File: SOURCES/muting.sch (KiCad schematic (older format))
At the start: 39 parts, among them Q1 BSH103,215, Q10 MMBF5434, Q11 MMBF5434, Q12 MMBF5434, Q13 BSS123, Q2 BSH103,215, Q3 BSH103,215, Q4 BSH103,215, Q5 BSH103,215, Q6 BSH103,215, Q7 BSH103,215, Q8 BSH103,215, Q9 MMBF5434, U1 SN74LVC3G14, U2 LM393, U3 LM393

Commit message: Updated schematics and labels
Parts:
- removed R1: 1k, symbol R
- added J4, J5, J6, J7: RCA_01, symbol RCA_01
- Q18: renamed from Q13; footprint (none) -> fdsp_housing_new:SOT-23
- renumbered C1 to C38, C2 to C39, C3 to C40, C4 to C41, C5 to C42, C6 to C43, C7 to C44, C8 to C45, C9 to C46, D5 to D10, D1 to D6, D2 to D7, D3 to D8, D4 to D9, Q5 to Q10, Q6 to Q11, Q7 to Q12, Q8 to Q13, Q9 to Q14, Q10 to Q15, Q11 to Q16, Q12 to Q17, Q1 to Q6, Q2 to Q7, Q3 to Q8, Q4 to Q9, R2 to R36, R3 to R37, R4 to R38, R5 to R39, R6 to R40, R7 to R41, R8 to R42, R9 to R43, U1 to U5, U2 to U6, U3 to U6
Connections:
- net +3V3: now also U6.6 (_); no longer U6.2 (_)
- net GND: now also C40.1, C41.1, U6.5 (+), J4.2 (GND), J5.2 (GND), J6.2 (GND), J7.2 (GND); no longer U6.3 (+)
- net CH1_OUT: no longer names the net of Q10.3 (D), Q14.1 (D)
- net CH1_OUT: now also J4.1 (SIG)
- net CH2_OUT: no longer names the net of Q11.3 (D), Q15.1 (D)
- net CH2_OUT: now also J5.1 (SIG)
- net CH3_OUT: no longer names the net of Q12.3 (D), Q16.1 (D)
- net CH3_OUT: now also J6.1 (SIG)
- net CH4_OUT: no longer names the net of Q13.3 (D), Q17.1 (D)
- net CH4_OUT: now also J7.1 (SIG)
- no-connect marks 0 -> 1

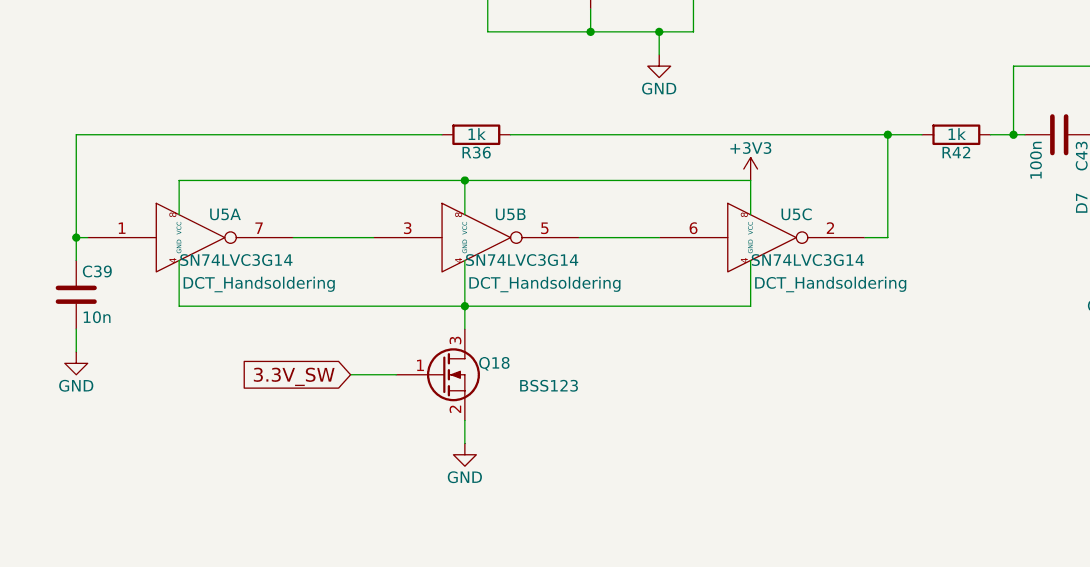
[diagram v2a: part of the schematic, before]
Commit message: Assigned footprints
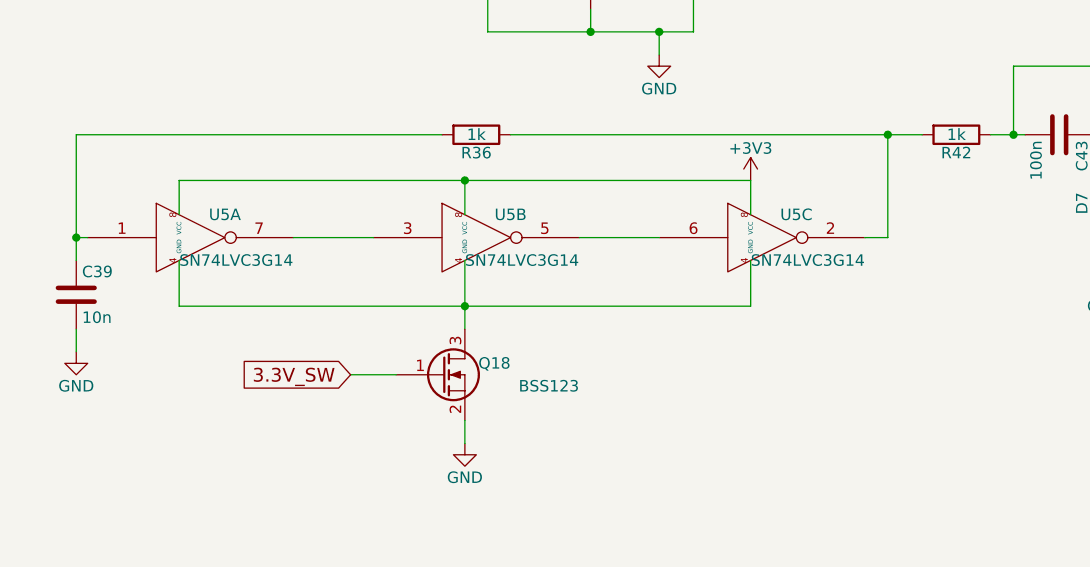
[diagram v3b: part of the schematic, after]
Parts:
- C38, C42: footprint (none) -> fdsp_capacitor:C_Radial_D5_L11_P2
- C39, C40, C41, C43, C44, C45, C46: footprint (none) -> fdsp_capacitor:C_1206_HandSoldering
- D10, D6, D7, D8, D9: footprint (none) -> fdsp_diode:SOD-123W
- J4, J5, J6, J7: footprint (none) -> fdsp_connector:RCA_RCJ-01x
- Q10, Q11, Q12, Q13, Q14, Q15, Q16, Q17, Q6, Q7, Q8, Q9: footprint TO_SOT_Packages_SMD:SOT-23_Handsoldering -> fdsp_housing_new:SOT-23_Handsoldering
- Q18: footprint fdsp_housing_new:SOT-23 -> fdsp_housing_new:SOT-23_Handsoldering
- R36, R37, R38, R39, R40, R41, R42, R43: footprint (none) -> fdsp_resistor:R_1206_HandSoldering
- U5: footprint DCT_Handsoldering -> fdsp_housing_new:DCT
- U6: footprint (none) -> fdsp_housing_new:SOIC-8_3.9x4.9mm_Pitch1.27mm

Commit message: updated schematic + bom + pcb start
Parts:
- added C42: 10u, fdsp_capacitor:C_Radial_D5_L11_P2, symbol CP
- added C43, C44: 100n, fdsp_capacitor:C_1206_HandSoldering, symbol C
- renumbered C38 to C45, C39 to C46, C40 to C47, C41 to C48, C42 to C49, C43 to C50, C44 to C51, C45 to C52, C46 to C53
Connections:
- net +3V3: now also C42.1, C43.2, C44.2
- net GND: now also C42.2, C43.1, C44.1
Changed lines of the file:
@@
 EESchema Schematic File Version 2
+LIBS:freeDSP_Classic_SMD-rescue
 LIBS:fdsp_device_new
 LIBS:fdsp_digital_new
@@
 $EndComp
 $Comp
-L C C39
+L C C46
 U 1 1 591CA7B6
 P 3950 4750
-F 0 "C39" H 3975 4850 50  0000 L CNN
+F 0 "C46" H 3975 4850 50  0000 L CNN
 F 1 "10n" H 3975 4650 50  0000 L CNN
 F 2 "fdsp_capacitor:C_1206_HandSoldering" H 3988 4600 50  0001 C CNN
@@
 $EndComp
 $Comp
-L GND #PWR073
+L GND #PWR075
 U 1 1 591CA831
 P 3950 5000
-F 0 "#PWR073" H 3950 4750 50  0001 C CNN
+F 0 "#PWR075" H 3950 4750 50  0001 C CNN
 F 1 "GND" H 3950 4850 50  0000 C CNN
 F 2 "" H 3950 5000 50  0001 C CNN
@@
 $EndComp
 $Comp
-L C C43
+L C C50
 U 1 1 591CA9EB
 P 8250 4050
-F 0 "C43" H 8275 4150 50  0000 L CNN
+F 0 "C50" H 8275 4150 50  0000 L CNN
 F 1 "100n" H 8275 3950 50  0000 L CNN
 F 2 "fdsp_capacitor:C_1206_HandSoldering" H 8288 3900 50  0001 C CNN
@@
 $EndComp
 $Comp
-L C C45
+L C C52
 U 1 1 591CAB8E
 P 9050 4350
-F 0 "C45" H 9075 4450 50  0000 L CNN
+F 0 "C52" H 9075 4450 50  0000 L CNN
 F 1 "100n" H 9075 4250 50  0000 L CNN
 F 2 "fdsp_capacitor:C_1206_HandSoldering" H 9088 4200 50  0001 C CNN
@@
 $EndComp
 $Comp
-L C C44
+L C C51
 U 1 1 591CAC8F
 P 9050 3750
-F 0 "C44" H 9075 3850 50  0000 L CNN
+F 0 "C51" H 9075 3850 50  0000 L CNN
 F 1 "100n" H 9075 3650 50  0000 L CNN
 F 2 "fdsp_capacitor:C_1206_HandSoldering" H 9088 3600 50  0001 C CNN
@@
 $EndComp
 $Comp
-L C C46
+L C C53
 U 1 1 591CACEA
 P 10100 4350
-F 0 "C46" H 10125 4450 50  0000 L CNN
+F 0 "C53" H 10125 4450 50  0000 L CNN
 F 1 "100n" H 10125 4250 50  0000 L CNN
 F 2 "fdsp_capacitor:C_1206_HandSoldering" H 10138 4200 50  0001 C CNN
@@
 $EndComp
 $Comp
-L GND #PWR074
+L GND #PWR076
 U 1 1 591CAE5F
 P 8450 4650
-F 0 "#PWR074" H 8450 4400 50  0001 C CNN
+F 0 "#PWR076" H 8450 4400 50  0001 C CNN
 F 1 "GND" H 8450 4500 50  0000 C CNN
 F 2 "" H 8450 4650 50  0001 C CNN
@@
 $EndComp
 $Comp
-L GND #PWR075
+L GND #PWR077
 U 1 1 591CAEB5
 P 9050 4650
-F 0 "#PWR075" H 9050 4400 50  0001 C CNN
+F 0 "#PWR077" H 9050 4400 50  0001 C CNN
 F 1 "GND" H 9050 4500 50  0000 C CNN
 F 2 "" H 9050 4650 50  0001 C CNN
@@
 $EndComp
 $Comp
-L GND #PWR076
+L GND #PWR078
 U 1 1 591CAEED
 P 10100 4650
-F 0 "#PWR076" H 10100 4400 50  0001 C CNN
+F 0 "#PWR078" H 10100 4400 50  0001 C CNN
 F 1 "GND" H 10100 4500 50  0000 C CNN
 F 2 "" H 10100 4650 50  0001 C CNN
@@
 $EndComp
 $Comp
-L GND #PWR077
+L GND #PWR079
 U 1 1 591CAF25
 P 10400 4650
-F 0 "#PWR077" H 10400 4400 50  0001 C CNN
+F 0 "#PWR079" H 10400 4400 50  0001 C CNN
 F 1 "GND" H 10400 4500 50  0000 C CNN
 F 2 "" H 10400 4650 50  0001 C CNN
@@
 $EndComp
 $Comp
-L GND #PWR078
+L GND #PWR080
 U 1 1 591CBEA2
 P 6500 3700
-F 0 "#PWR078" H 6500 3450 50  0001 C CNN
+F 0 "#PWR080" H 6500 3450 50  0001 C CNN
 F 1 "GND" H 6500 3550 50  0000 C CNN
 F 2 "" H 6500 3700 50  0001 C CNN
@@
 $EndComp
 $Comp
-L +3V3 #PWR079
+L +3V3 #PWR081
 U 1 1 591CBF58
 P 6500 2250
-F 0 "#PWR079" H 6500 2100 50  0001 C CNN
+F 0 "#PWR081" H 6500 2100 50  0001 C CNN
 F 1 "+3V3" H 6500 2390 50  0000 C CNN
 F 2 "" H 6500 2250 50  0001 C CNN
@@
 $EndComp
 $Comp
-L CP C42
+L CP C49
 U 1 1 591CC026
 P 5750 3150
-F 0 "C42" H 5775 3250 50  0000 L CNN
+F 0 "C49" H 5775 3250 50  0000 L CNN
 F 1 "2.2u" H 5775 3050 50  0000 L CNN
 F 2 "fdsp_capacitor:C_Radial_D5_L11_P2" H 5788 3000 50  0001 C CNN
@@
 3.3V_SW
 $Comp
-L +3V3 #PWR080
+L +3V3 #PWR082
 U 1 1 591CD35F
 P 3950 2600
-F 0 "#PWR080" H 3950 2450 50  0001 C CNN
+F 0 "#PWR082" H 3950 2450 50  0001 C CNN
 F 1 "+3V3" H 3950 2740 50  0000 C CNN
 F 2 "" H 3950 2600 50  0001 C CNN
@@
 $EndComp
 $Comp
-L GND #PWR081
+L GND #PWR083
 U 1 1 591CD3C2
 P 3950 3100
-F 0 "#PWR081" H 3950 2850 50  0001 C CNN
+F 0 "#PWR083" H 3950 2850 50  0001 C CNN
 F 1 "GND" H 3950 2950 50  0000 C CNN
 F 2 "" H 3950 3100 50  0001 C CNN
@@
 $EndComp
 $Comp
-L CP C38
+L CP C45
 U 1 1 591CD40F
 P 3950 2850
-F 0 "C38" H 3975 2950 50  0000 L CNN
+F 0 "C45" H 3975 2950 50  0000 L CNN
 F 1 "10u" H 3975 2750 50  0000 L CNN
 F 2 "fdsp_capacitor:C_Radial_D5_L11_P2" H 3988 2700 50  0001 C CNN
@@
 $EndComp
 $Comp
-L C C40
+L C C47
 U 1 1 591CD4D7
 P 4350 2850
-F 0 "C40" H 4375 2950 50  0000 L CNN
+F 0 "C47" H 4375 2950 50  0000 L CNN
 F 1 "100n" H 4375 2750 50  0000 L CNN
 F 2 "fdsp_capacitor:C_1206_HandSoldering" H 4388 2700 50  0001 C CNN
@@
 $EndComp
 $Comp
-L C C41
+L C C48
 U 1 1 591CD58D
 P 4700 2850
-F 0 "C41" H 4725 2950 50  0000 L CNN
+F 0 "C48" H 4725 2950 50  0000 L CNN
 F 1 "100n" H 4725 2750 50  0000 L CNN
 F 2 "fdsp_capacitor:C_1206_HandSoldering" H 4738 2700 50  0001 C CNN
@@
 $EndComp
 $Comp
-L GND #PWR082
+L GND #PWR084
 U 1 1 591CE75B
 P 2550 2350
-F 0 "#PWR082" H 2550 2100 50  0001 C CNN
+F 0 "#PWR084" H 2550 2100 50  0001 C CNN
 F 1 "GND" H 2550 2200 50  0000 C CNN
 F 2 "" H 2550 2350 50  0001 C CNN
@@
 $EndComp
 $Comp
-L GND #PWR083
+L GND #PWR085
 U 1 1 591D04F3
 P 2550 3850
-F 0 "#PWR083" H 2550 3600 50  0001 C CNN
+F 0 "#PWR085" H 2550 3600 50  0001 C CNN
 F 1 "GND" H 2550 3700 50  0000 C CNN
 F 2 "" H 2550 3850 50  0001 C CNN
@@
 $EndComp
 $Comp
-L GND #PWR084
+L GND #PWR086
 U 1 1 591D0943
 P 2550 5600
-F 0 "#PWR084" H 2550 5350 50  0001 C CNN
+F 0 "#PWR086" H 2550 5350 50  0001 C CNN
 F 1 "GND" H 2550 5450 50  0000 C CNN
 F 2 "" H 2550 5600 50  0001 C CNN
@@
 $EndComp
 $Comp
-L GND #PWR085
+L GND #PWR087
 U 1 1 591D096B
 P 2550 7100
-F 0 "#PWR085" H 2550 6850 50  0001 C CNN
+F 0 "#PWR087" H 2550 6850 50  0001 C CNN
 F 1 "GND" H 2550 6950 50  0000 C CNN
 F 2 "" H 2550 7100 50  0001 C CNN
@@
 $EndComp
 $Comp
-L GND #PWR086
+L GND #PWR088
 U 1 1 59234CC3
 P 6500 1800
-F 0 "#PWR086" H 6500 1550 50  0001 C CNN
+F 0 "#PWR088" H 6500 1550 50  0001 C CNN
 F 1 "GND" H 6500 1650 50  0000 C CNN
 F 2 "" H 6500 1800 50  0001 C CNN
@@
 $EndComp
 $Comp
-L +3V3 #PWR087
+L +3V3 #PWR089
 U 1 1 59234EBA
 P 6500 1000
-F 0 "#PWR087" H 6500 850 50  0001 C CNN
+F 0 "#PWR089" H 6500 850 50  0001 C CNN
 F 1 "+3V3" H 6500 1140 50  0000 C CNN
 F 2 "" H 6500 1000 50  0001 C CNN
@@
 $EndComp
 $Comp
-L +3V3 #PWR088
+L +3V3 #PWR090
 U 1 1 5923579B
 P 6900 4250
-F 0 "#PWR088" H 6900 4100 50  0001 C CNN
+F 0 "#PWR090" H 6900 4100 50  0001 C CNN
 F 1 "+3V3" H 6900 4390 50  0000 C CNN
 F 2 "" H 6900 4250 50  0001 C CNN
@@
 $EndComp
 $Comp
-L GND #PWR089
+L GND #PWR091
 U 1 1 59235E08
 P 5650 5400
-F 0 "#PWR089" H 5650 5150 50  0001 C CNN
+F 0 "#PWR091" H 5650 5150 50  0001 C CNN
 F 1 "GND" H 5650 5250 50  0000 C CNN
 F 2 "" H 5650 5400 50  0001 C CNN
@@
 $EndComp
 $Comp
-L GND #PWR090
+L GND #PWR092
 U 1 1 5932C8F1
 P 2750 1600
-F 0 "#PWR090" H 2750 1350 50  0001 C CNN
+F 0 "#PWR092" H 2750 1350 50  0001 C CNN
 F 1 "GND" H 2750 1450 50  0000 C CNN
 F 2 "" H 2750 1600 60  0000 C CNN
@@
 $EndComp
 $Comp
-L GND #PWR091
+L GND #PWR093
 U 1 1 5932D0B8
 P 2750 6350
-F 0 "#PWR091" H 2750 6100 50  0001 C CNN
+F 0 "#PWR093" H 2750 6100 50  0001 C CNN
 F 1 "GND" H 2750 6200 50  0000 C CNN
 F 2 "" H 2750 6350 60  0000 C CNN
@@
 $EndComp
 $Comp
-L GND #PWR092
+L GND #PWR094
 U 1 1 5932D1C1
 P 2750 4850
-F 0 "#PWR092" H 2750 4600 50  0001 C CNN
+F 0 "#PWR094" H 2750 4600 50  0001 C CNN
 F 1 "GND" H 2750 4700 50  0000 C CNN
 F 2 "" H 2750 4850 60  0000 C CNN
@@
 $EndComp
 $Comp
-L GND #PWR093
+L GND #PWR095
 U 1 1 5932D22F
 P 2750 3100
-F 0 "#PWR093" H 2750 2850 50  0001 C CNN
+F 0 "#PWR095" H 2750 2850 50  0001 C CNN
 F 1 "GND" H 2750 2950 50  0000 C CNN
 F 2 "" H 2750 3100 60  0000 C CNN
@@
 Wire Wire Line
 	3950 3050 4700 3050
+$Comp
+L +3V3 #PWR096
+U 1 1 592EDB90
+P 2350 950
+F 0 "#PWR096" H 2350 800 50  0001 C CNN
+F 1 "+3V3" H 2350 1090 50  0000 C CNN
+F 2 "" H 2350 950 50  0001 C CNN
+F 3 "" H 2350 950 50  0001 C CNN
+	1    2350 950
+	1    0    0    -1
+$EndComp
+$Comp
+L GND #PWR097
+U 1 1 592EDB96
+P 2350 1450
+F 0 "#PWR097" H 2350 1200 50  0001 C CNN
+F 1 "GND" H 2350 1300 50  0000 C CNN
+F 2 "" H 2350 1450 50  0001 C CNN
+F 3 "" H 2350 1450 50  0001 C CNN
+	1    2350 1450
+	1    0    0    -1
+$EndComp
+$Comp
+L CP C42
+U 1 1 592EDB9C
+P 2350 1200
+F 0 "C42" H 2375 1300 50  0000 L CNN
+F 1 "10u" H 2375 1100 50  0000 L CNN
+F 2 "fdsp_capacitor:C_Radial_D5_L11_P2" H 2388 1050 50  0001 C CNN
+F 3 "" H 2350 1200 50  0001 C CNN
+	1    2350 1200
+	1    0    0    -1
+$EndComp
+$Comp
+L C C43
+U 1 1 592EDBA2
+P 2750 1200
+F 0 "C43" H 2775 1300 50  0000 L CNN
+F 1 "100n" H 2775 1100 50  0000 L CNN
+F 2 "fdsp_capacitor:C_1206_HandSoldering" H 2788 1050 50  0001 C CNN
+F 3 "" H 2750 1200 50  0001 C CNN
+	1    2750 1200
+	-1   0    0    1
+$EndComp
+$Comp
+L C C44
+U 1 1 592EDBA8
+P 3100 1200
+F 0 "C44" H 3125 1300 50  0000 L CNN
+F 1 "100n" H 3125 1100 50  0000 L CNN
+F 2 "fdsp_capacitor:C_1206_HandSoldering" H 3138 1050 50  0001 C CNN
+F 3 "" H 3100 1200 50  0001 C CNN
+	1    3100 1200
+	-1   0    0    1
+$EndComp
+Wire Wire Line
+	2350 950  2350 1050
+Wire Wire Line
+	2350 1350 2350 1450
+Wire Wire Line
+	2750 1050 2750 1000
+Connection ~ 2350 1000
+Wire Wire Line
+	3100 1000 3100 1050
+Connection ~ 2750 1000
+Wire Wire Line
+	3100 1400 3100 1350
+Wire Wire Line
+	2750 1400 2750 1350
+Connection ~ 2750 1400
+Connection ~ 2350 1400
+Wire Wire Line
+	2350 1000 3100 1000
+Wire Wire Line
+	2350 1400 3100 1400
 $EndSCHEMATC

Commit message: fixed switched GND Q18, placed some components
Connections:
- net GND_SW: now reaches Q18.3 (D), U5.4 (GND), U5.4 (GND), U5.4 (GND)
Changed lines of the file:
@@
 Wire Wire Line
 	2350 1400 3100 1400
+Text Label 5975 4800 0    60   ~ 0
+GND_SW
 $EndSCHEMATC

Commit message: layout finished
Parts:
- removed C42: 10u, fdsp_capacitor:C_Radial_D5_L11_P2, symbol CP
- removed C43, C44: 100n, fdsp_capacitor:C_1206_HandSoldering, symbol C
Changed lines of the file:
@@
 Wire Wire Line
 	3950 3050 4700 3050
-$Comp
-L +3V3 #PWR096
-U 1 1 592EDB90
-P 2350 950
-F 0 "#PWR096" H 2350 800 50  0001 C CNN
-F 1 "+3V3" H 2350 1090 50  0000 C CNN
-F 2 "" H 2350 950 50  0001 C CNN
-F 3 "" H 2350 950 50  0001 C CNN
-	1    2350 950
-	1    0    0    -1
-$EndComp
-$Comp
-L GND #PWR097
-U 1 1 592EDB96
-P 2350 1450
-F 0 "#PWR097" H 2350 1200 50  0001 C CNN
-F 1 "GND" H 2350 1300 50  0000 C CNN
-F 2 "" H 2350 1450 50  0001 C CNN
-F 3 "" H 2350 1450 50  0001 C CNN
-	1    2350 1450
-	1    0    0    -1
-$EndComp
-$Comp
-L CP C42
-U 1 1 592EDB9C
-P 2350 1200
-F 0 "C42" H 2375 1300 50  0000 L CNN
-F 1 "10u" H 2375 1100 50  0000 L CNN
-F 2 "fdsp_capacitor:C_Radial_D5_L11_P2" H 2388 1050 50  0001 C CNN
-F 3 "" H 2350 1200 50  0001 C CNN
-	1    2350 1200
-	1    0    0    -1
-$EndComp
-$Comp
-L C C43
-U 1 1 592EDBA2
-P 2750 1200
-F 0 "C43" H 2775 1300 50  0000 L CNN
-F 1 "100n" H 2775 1100 50  0000 L CNN
-F 2 "fdsp_capacitor:C_1206_HandSoldering" H 2788 1050 50  0001 C CNN
-F 3 "" H 2750 1200 50  0001 C CNN
-	1    2750 1200
-	-1   0    0    1
-$EndComp
-$Comp
-L C C44
-U 1 1 592EDBA8
-P 3100 1200
-F 0 "C44" H 3125 1300 50  0000 L CNN
-F 1 "100n" H 3125 1100 50  0000 L CNN
-F 2 "fdsp_capacitor:C_1206_HandSoldering" H 3138 1050 50  0001 C CNN
-F 3 "" H 3100 1200 50  0001 C CNN
-	1    3100 1200
-	-1   0    0    1
-$EndComp
-Wire Wire Line
-	2350 950  2350 1050
-Wire Wire Line
-	2350 1350 2350 1450
-Wire Wire Line
-	2750 1050 2750 1000
-Connection ~ 2350 1000
-Wire Wire Line
-	3100 1000 3100 1050
-Connection ~ 2750 1000
-Wire Wire Line
-	3100 1400 3100 1350
-Wire Wire Line
-	2750 1400 2750 1350
-Connection ~ 2750 1400
-Connection ~ 2350 1400
-Wire Wire Line
-	2350 1000 3100 1000
-Wire Wire Line
-	2350 1400 3100 1400
 Text Label 5975 4800 0    60   ~ 0
 GND_SW
